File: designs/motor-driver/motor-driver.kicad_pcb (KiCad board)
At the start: 2 copper layers, 50 x 50 mm, 16 parts, among them IC1 ATMEGA168-P, P1 CONN_2, P2 ISP, P3 CONN_2, P4 CONN_2, P5 CONN_2, P6 CONN_2, U1 TB6552FNG, U2 TB6552FNG, X1 CRYSTAL_RESONATOR

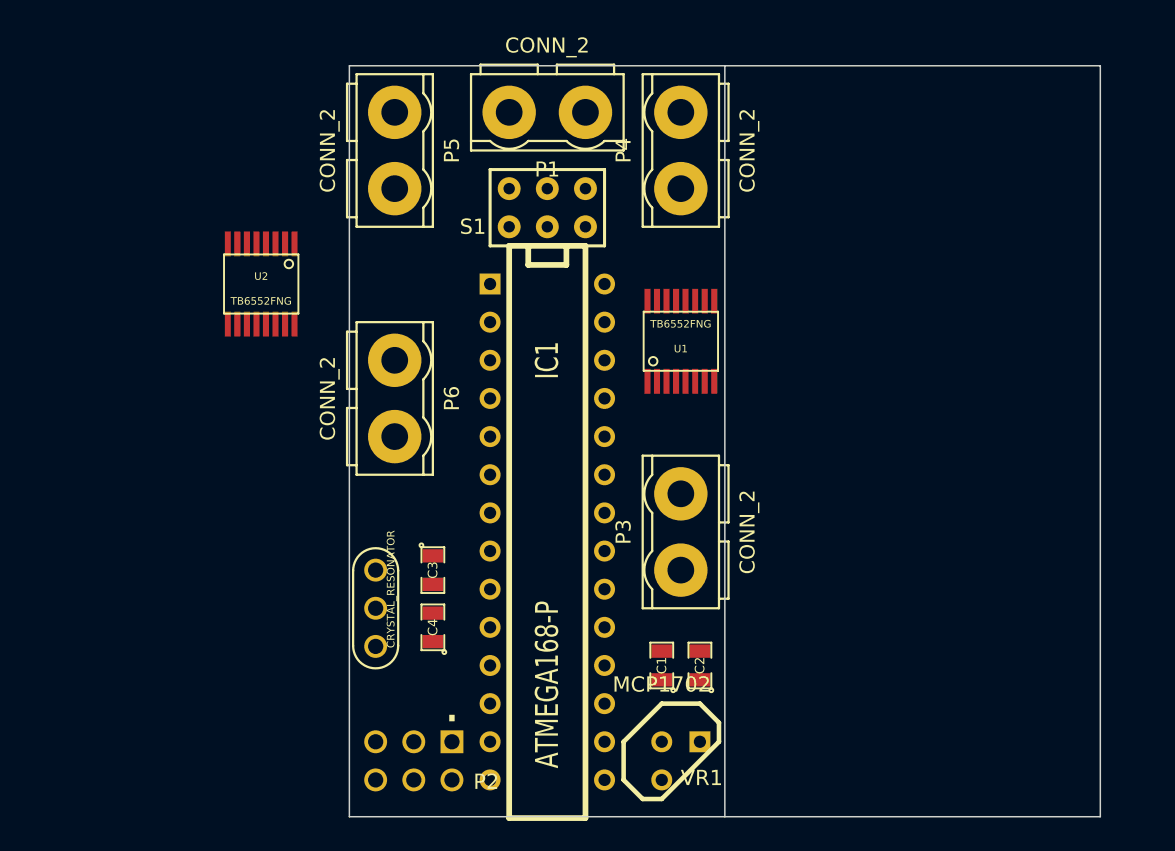
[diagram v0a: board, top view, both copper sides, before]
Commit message: Changed to L293D chip... a bit easier to work with, and has tons of support with AVR / Arduino code.
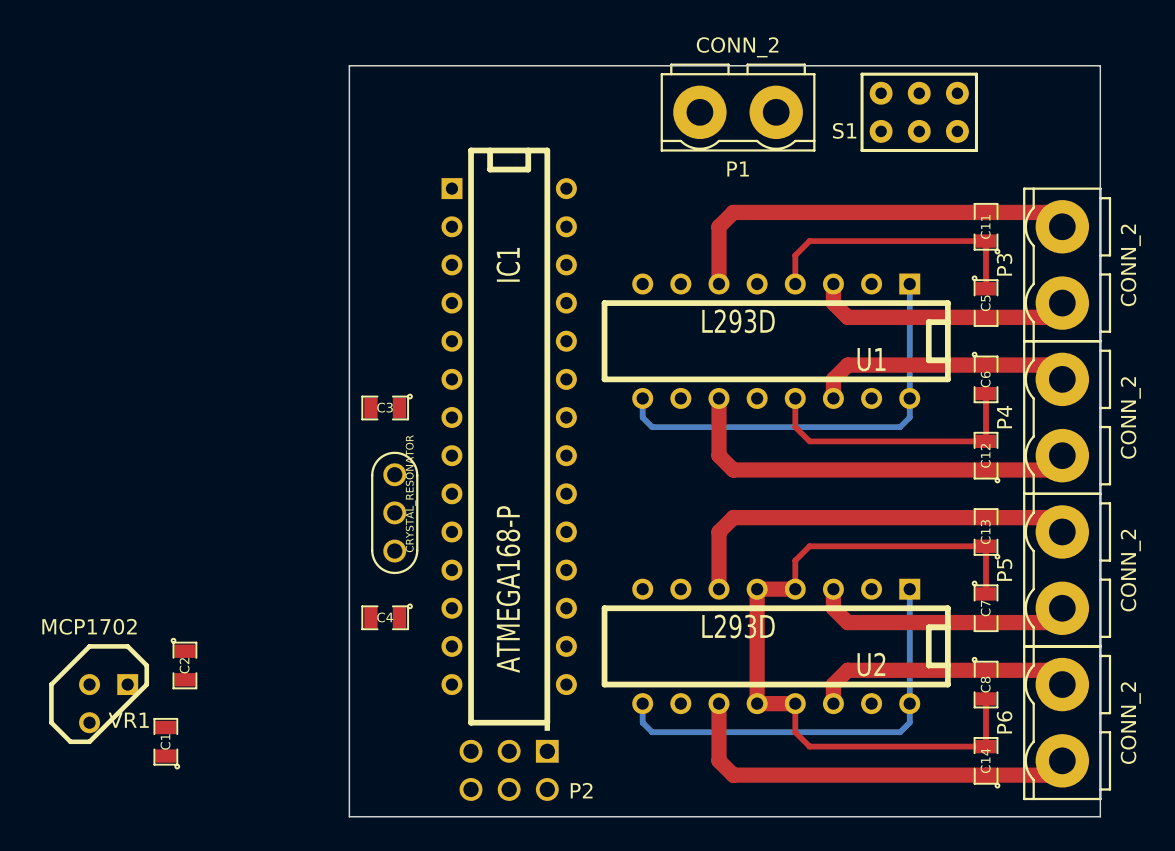
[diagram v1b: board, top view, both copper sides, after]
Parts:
- added C11: 0.1uF, SM0805, F.Cu at (72.4, 45.7)
- added C12: 0.1uF, SM0805, F.Cu at (72.4, 61.0)
- added C13: 0.1uF, SM0805, F.Cu at (72.4, 66.0)
- added C14: 0.1uF, SM0805, F.Cu at (72.4, 81.3)
- added C5: 0.1uF, SM0805, F.Cu at (72.4, 50.8)
- added C6: 0.1uF, SM0805, F.Cu at (72.4, 55.9)
- added C7: 0.1uF, SM0805, F.Cu at (72.4, 71.1)
- added C8: 0.1uF, SM0805, F.Cu at (72.4, 76.2)
- U1, U2: value TB6552FNG -> L293D; footprint ssop-16 -> DIP-16__300
- moved P5 52.5 mm to (77.5, 68.6), turned to 90 degrees
- moved P6 49.4 mm to (77.5, 78.7), turned to 90 degrees
- moved U2 41.9 mm to (58.4, 73.7)
- moved VR1 38.3 mm to (14.0, 77.5)
- moved C2 34.3 mm to (19.1, 74.9), turned to 270 degrees
- moved C1 33.4 mm to (17.8, 80.0)
- moved P3 31.0 mm to (77.5, 48.3)
- moved P4 31.0 mm to (77.5, 58.4)
- moved S1 25.6 mm to (67.9, 38.1)
- moved P1 12.7 mm to (55.9, 38.1)
- moved C3 11.3 mm to (32.4, 57.8), turned to 180 degrees
- moved IC1 6.84 mm to (40.6, 59.7)
- moved X1 6.48 mm to (33.0, 64.8)
- moved P2 6.38 mm to (40.6, 81.9)
- moved U1 6.35 mm to (58.4, 53.3), turned to 180 degrees
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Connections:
- net /AIN1 renamed /MOTOR1_1A
- net /BO1 renamed /MOTOR2_3Y
- net /DO1 renamed /MOTOR4_3Y
- net N-000004 renamed /VREG_IN
- C1 pad 1: +3.3V -> /VREG_OUT
- IC1 pad 11: /DIN1 -> (no net)
- IC1 pad 12: /DIN2 -> (no net)
- IC1 pad 13: /DPWM -> (no net)
- IC1 pad 15: /APWM -> /MOTOR2_4A
- IC1 pad 16: /AIN2 -> /MOTOR2_3A
- IC1 pad 23: /BIN1 -> /MOTOR1_2A
- IC1 pad 24: /BIN2 -> /MOTOR3_1A
- IC1 pad 25: /BPWM -> /MOTOR3_2A
- IC1 pad 26: (no net) -> /MOTOR4_3A
- IC1 pad 4: /CIN1 -> (no net)
- IC1 pad 5: /CIN2 -> /MOTOR4_4A
- IC1 pad 6: /CPWM -> (no net)
- P3 pad 1: /AO1 -> /MOTOR1_1Y
- P3 pad 2: /AO2 -> /MOTOR1_2Y
- P4 pad 2: /BO2 -> /MOTOR2_4Y
- P5 pad 1: /CO1 -> /MOTOR3_1Y
- P5 pad 2: /CO2 -> /MOTOR3_2Y
- P6 pad 2: /DO2 -> /MOTOR4_4Y
- S1 pad 6: +3.3V -> /VREG_OUT
- U1 pad 1: GND -> +5V
- U1 pad 10: /BO2 -> /MOTOR2_3A
- U1 pad 12: +3.3V -> GND
- U1 pad 13: /BPWM -> GND
- U1 pad 14: /BIN2 -> /MOTOR2_4Y
- U1 pad 15: /BIN1 -> /MOTOR2_4A
- U1 pad 16: +3.3V -> +5V
- U1 pad 3: /AIN2 -> /MOTOR1_1Y
- U1 pad 4: /APWM -> GND
- U1 pad 5: +3.3V -> GND
- U1 pad 6: +6V -> /MOTOR1_2Y
- U1 pad 7: /AO1 -> /MOTOR1_2A
- U1 pad 8: /AO2 -> +BATT
- U1 pad 9: AGND -> +5V
- U2 pad 1: GND -> +5V
- U2 pad 10: /DO2 -> /MOTOR4_3A
- U2 pad 12: +3.3V -> GND
- U2 pad 13: /DPWM -> GND
- U2 pad 14: /DIN2 -> /MOTOR4_4Y
- U2 pad 15: /DIN1 -> /MOTOR4_4A
- U2 pad 16: +3.3V -> +5V
- U2 pad 2: /CIN1 -> /MOTOR3_1A
- U2 pad 3: /CIN2 -> /MOTOR3_1Y
- U2 pad 4: /CPWM -> GND
- U2 pad 5: +3.3V -> GND
- U2 pad 6: +6V -> /MOTOR3_2Y
- U2 pad 7: /CO1 -> /MOTOR3_2A
- U2 pad 8: /CO2 -> +BATT
- U2 pad 9: AGND -> +5V
- VR1 pad 3: +3.3V -> /VREG_OUT
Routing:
- net GND: track 0.00 -> 85.4 mm
- net +5V: track 0.00 -> 56.9 mm
- net /MOTOR4_3Y: track 0.00 -> 27.5 mm
- net /MOTOR2_3Y: track 0.00 -> 27.5 mm
- net /MOTOR1_2Y: track 0.00 -> 27.5 mm
- net /MOTOR3_2Y: track 0.00 -> 27.5 mm
- net /MOTOR3_1Y: track 0.00 -> 17.3 mm
- net /MOTOR4_4Y: track 0.00 -> 17.3 mm
- net /MOTOR2_4Y: track 0.00 -> 17.3 mm
- net /MOTOR1_1Y: track 0.00 -> 17.3 mm
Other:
- outline, holes or cut-outs redrawn
- net class Default: clearance 0.254 -> 0.381; trace_width 0.254 -> 0.381
- rule trace_clearance: 0.254 -> 0.381
- rule trace_min: 0.254 -> 0.381

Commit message: annoying through hole, 5v components...
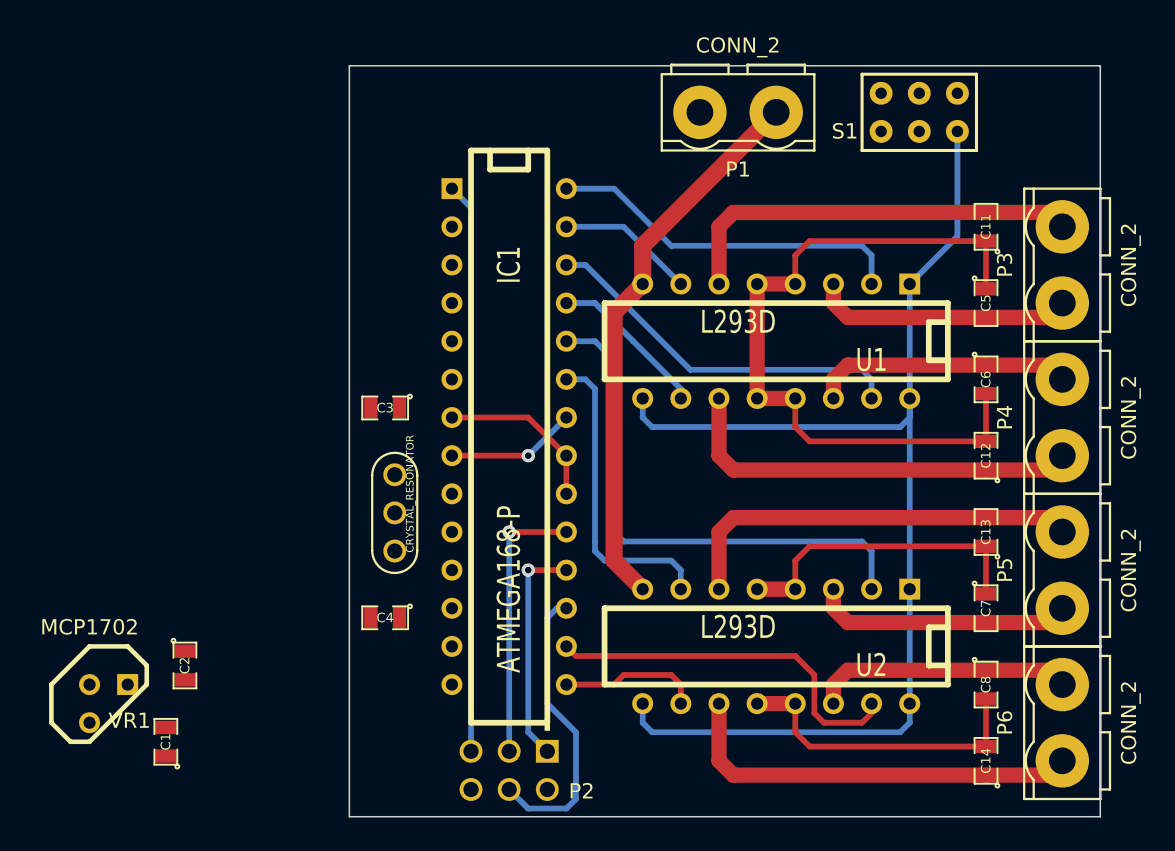
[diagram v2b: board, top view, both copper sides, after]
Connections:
- net N-0000032 renamed /PROG_VCC
- C1 pad 1: /VREG_OUT -> +5V
- IC1 pad 14: /MOTOR1_1A -> (no net)
- IC1 pad 15: /MOTOR2_4A -> /MOTOR4_3A
- IC1 pad 16: /MOTOR2_3A -> /MOTOR4_4A
- IC1 pad 23: /MOTOR1_2A -> /MOTOR3_2A
- IC1 pad 25: /MOTOR3_2A -> /MOTOR2_3A
- IC1 pad 26: /MOTOR4_3A -> /MOTOR2_4A
- IC1 pad 27: (no net) -> /MOTOR1_2A
- IC1 pad 28: (no net) -> /MOTOR1_1A
- IC1 pad 5: /MOTOR4_4A -> (no net)
- S1 pad 6: /VREG_OUT -> +5V
- VR1 pad 3: /VREG_OUT -> +5V
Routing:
- net /RESET: track 0.00 -> 38.0 mm
- net +BATT: track 0.00 -> 37.0 mm
- net /MOTOR3_1A: track 0.00 -> 35.3 mm
- net /MOTOR4_4A: track 0.00 -> 24.8 mm
- net /MOTOR2_4A: track 0.00 -> 24.7 mm
- net +5V: track 56.9 -> 81.1 mm
- net /MOTOR1_1A: track 0.00 -> 24.1 mm
- net /MOTOR3_2A: track 0.00 -> 20.5 mm
- net /MOSI: track 0.00 -> 19.6 mm
- net /SCK: track 0.00 -> 18.4 mm, vias 0 -> 1
- net /MISO: track 0.00 -> 15.1 mm, vias 0 -> 1
- net GND: track 85.4 -> 99.2 mm, vias 0 -> 1
- net VCC: track 0.00 -> 11.2 mm
- net /MOTOR2_3A: track 0.00 -> 10.6 mm
- net /MOTOR4_3A: track 0.00 -> 9.42 mm
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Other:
- net class Default: clearance 0.381 -> 0.254
- rule trace_clearance: 0.381 -> 0.254

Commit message: WIP motor driver... adding XBee, optional 5v regulator, etc
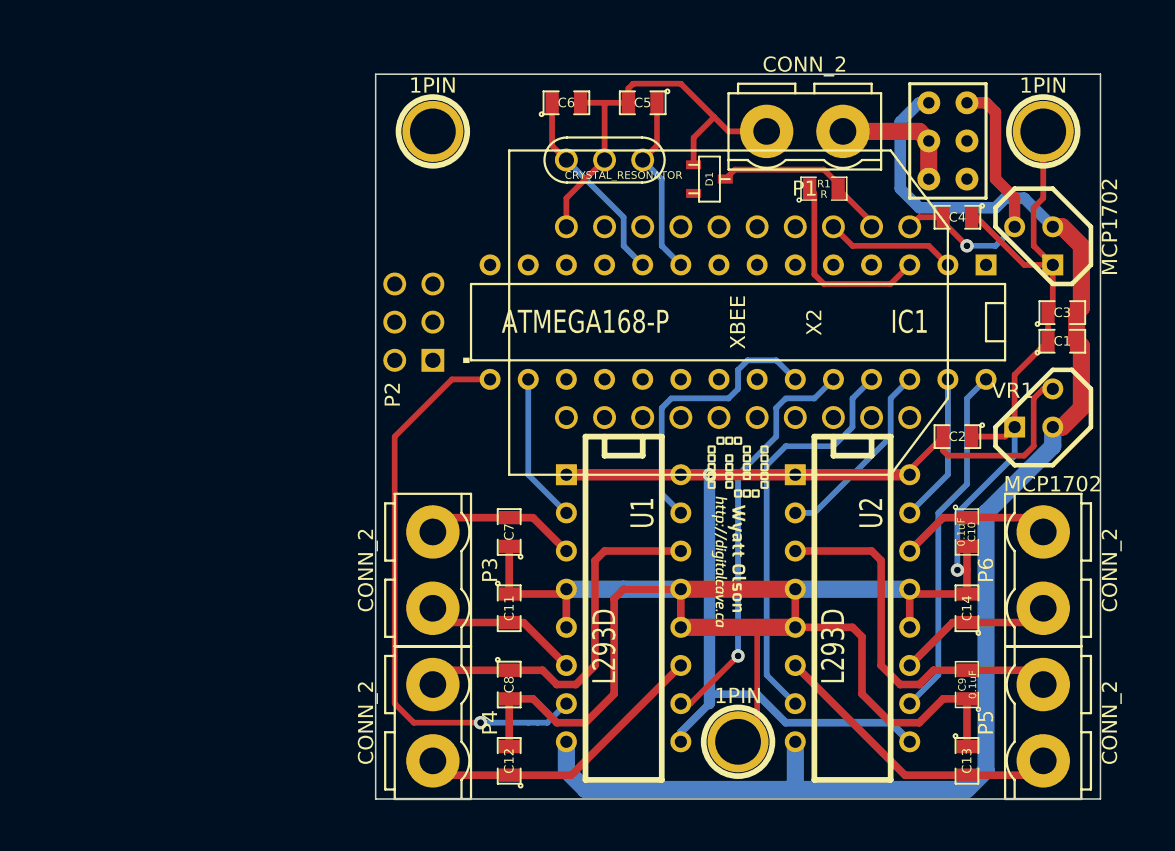
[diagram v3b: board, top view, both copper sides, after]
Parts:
- added 1PIN: P***, 1pin, F.Cu at (55.9, 80.0)
- added 1PIN: P***, 1pin, F.Cu at (35.6, 39.4)
- added 1PIN: P***, 1pin, F.Cu at (76.2, 39.4)
- added C10: 0.1uF, SM0805, F.Cu at (71.1, 66.0)
- added C9: 0.1uF, SM0805, F.Cu at (71.1, 76.2)
- added D1: ZENER, sot23, F.Cu at (54.0, 42.5)
- added R1: R, SM0805, F.Cu at (61.6, 43.2)
- added VAL: DIGITALCAVE_LOGO_WIDE_SMALL, DIGITALCAVE_LOGO_WIDE_SMALL, F.Cu at (55.9, 66.0)
- added VR2: MCP1702, TO92, F.Cu at (75.6, 47.0)
- added X2: XBEE, XBEE_SPARKFUN_BREAKOUT, F.Cu at (55.9, 52.1)
- C1, C2, C3, C4: value C -> 1uF
- C5, C6: value 0.1uF -> 20pF
- moved C1 65.4 mm to (77.5, 53.3), turned to 0 degrees
- moved VR1 64.7 mm to (75.6, 57.8), turned to 180 degrees
- moved C2 53.6 mm to (70.5, 59.7), turned to 180 degrees
- moved P3 46.6 mm to (35.6, 68.6), turned to 270 degrees
- moved P4 46.6 mm to (35.6, 78.7), turned to 270 degrees
- moved C4 46.5 mm to (70.5, 45.1)
- moved C3 45.5 mm to (77.5, 51.4), turned to 0 degrees
- moved C11 40.7 mm to (40.6, 71.1), turned to 270 degrees
- moved C12 37.7 mm to (40.6, 81.3)
- moved C6 33.5 mm to (44.5, 37.5), turned to 0 degrees
- moved C7 32.2 mm to (40.6, 66.0), turned to 90 degrees
- moved C8 31.8 mm to (40.6, 76.2)
- moved P2 30.5 mm to (34.3, 52.1), turned to 90 degrees
- moved X1 27.3 mm to (47.0, 41.3), turned to 180 degrees
- moved C5 26.5 mm to (49.5, 37.5), turned to 180 degrees
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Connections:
- net /PROG_VCC renamed N-0000011
- net VCC renamed N-0000047
- C1 pad 1: +5V -> GND
- C1 pad 2: GND -> +BATT
- C2 pad 1: /VREG_IN -> GND
- C2 pad 2: GND -> +5V
- C3 pad 1: /XTAL1 -> GND
- C3 pad 2: GND -> +BATT
- C4 pad 1: /XTAL2 -> GND
- C4 pad 2: GND -> +3.3V
- C5 pad 1: GND -> /XTAL1
- C5 pad 2: /MOTOR1_1Y -> GND
- C6 pad 1: /MOTOR2_4Y -> /XTAL2
- C7 pad 2: /MOTOR3_1Y -> /MOTOR1_1Y
- C8 pad 1: /MOTOR4_4Y -> /MOTOR2_4Y
- IC1 pad 15: /MOTOR4_3A -> /MOTOR1_2A
- IC1 pad 16: /MOTOR4_4A -> /MOTOR1_1A
- IC1 pad 2: (no net) -> N-0000037
- IC1 pad 23: /MOTOR3_2A -> /MOTOR2_4A
- IC1 pad 24: /MOTOR3_1A -> /MOTOR2_3A
- IC1 pad 25: /MOTOR2_3A -> /MOTOR3_2A
- IC1 pad 26: /MOTOR2_4A -> /MOTOR3_1A
- IC1 pad 27: /MOTOR1_2A -> /MOTOR4_4A
- IC1 pad 28: /MOTOR1_1A -> /MOTOR4_3A
- IC1 pad 3: (no net) -> N-0000019
- P1 pad 1: +BATT -> N-0000039
- P4 pad 1: /MOTOR2_3Y -> /MOTOR2_4Y
- P4 pad 2: /MOTOR2_4Y -> /MOTOR2_3Y
- P5 pad 1: /MOTOR3_1Y -> /MOTOR3_2Y
- P5 pad 2: /MOTOR3_2Y -> /MOTOR3_1Y
- S1 pad 1: /VREG_IN -> N-0000039
- S1 pad 2: +BATT -> N-0000039
- S1 pad 3: (no net) -> +BATT
- S1 pad 6: +5V -> +3.3V
- VR1 pad 2: /VREG_IN -> +BATT
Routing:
- net GND: track 99.2 -> 176.7 mm
- net +BATT: track 37.0 -> 93.3 mm
- net /RESET: track 38.0 -> 0.00 mm
- net /MOTOR1_2A: track 9.20 -> 38.2 mm, vias 0 -> 1
- net /MOTOR3_1A: track 35.3 -> 12.8 mm
- net /MOSI: track 19.6 -> 0.00 mm
- net +3.3V: track 0.00 -> 19.1 mm, vias 0 -> 1
- net /SCK: track 18.4 -> 0.00 mm, vias 1 -> 0
- net /MOTOR4_3Y: track 27.5 -> 10.5 mm
- net /MOTOR1_2Y: track 27.5 -> 10.5 mm
- net /MOTOR2_3A: track 10.6 -> 27.3 mm, vias 0 -> 1
- net /MISO: track 15.1 -> 0.00 mm, vias 1 -> 0
- net /MOTOR4_4A: track 24.8 -> 9.94 mm
- net /MOTOR4_3A: track 9.42 -> 23.7 mm
- net /MOTOR1_1A: track 24.1 -> 9.94 mm
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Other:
- board size 50 x 50 mm -> 48.3 x 48.3 mm

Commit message: More updates to motor circuit.  Finished adding XBee, added LED, cleaned up text, etc.
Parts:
- removed the 1PIN at (35.6, 39.4)
- added D2: LED, LED-5MM, F.Cu at (36.2, 59.7)
- added P7: CONN_7, PIN_ARRAY_7x1, F.Cu at (54.6, 37.5)
- added R2: 1k, SM0805, F.Cu at (40.6, 59.1)
- D1: value ZENER -> ZD 3v3
- P1: value CONN_2 -> BATT
- P3: value CONN_2 -> MOTOR_1
- P4: value CONN_2 -> MOTOR_2
- P5: value CONN_2 -> MOTOR_3
- P6: value CONN_2 -> MOTOR_4
- R1: value R -> 1k
- VR1, VR2: footprint TO92 -> TO92_SMALL
- moved 1PIN 21.7 mm to (54.6, 41.3)
- moved P1 16.6 mm to (76.8, 41.3), turned to 90 degrees
- moved C5 11.0 mm to (38.7, 39.4)
- moved C3 10.8 mm to (78.1, 62.2)
- moved X1 10.3 mm to (36.8, 43.2)
- moved C4 10.0 mm to (76.2, 53.3), turned to 0 degrees
- moved C6 9.71 mm to (34.9, 39.4)
- moved C1 9.53 mm to (71.8, 45.7), turned to 180 degrees
- moved D1 8.25 mm to (62.2, 42.5)
- moved C2 4.58 mm to (74.3, 62.2)
- moved R1 4.49 mm to (66.0, 42.5), turned to 180 degrees
- moved VAL 3.81 mm to (55.9, 69.8), turned to 90 degrees
- moved VR2 2.62 mm to (76.2, 49.5)
- moved S1 1.27 mm to (71.1, 40.0), turned to 270 degrees
- moved VR1 0.64 mm to (76.2, 57.8), turned to 270 degrees
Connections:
- net N-0000011 renamed /PROG_VCC
- net N-0000019 renamed /TX
- net N-0000047 renamed /AVR_VCC
- D1 pad 2: N-0000018 -> N-0000034
- IC1 pad 11: (no net) -> /MOTOR2_4A
- IC1 pad 2: N-0000037 -> /RX
- IC1 pad 23: /MOTOR2_4A -> /ADC0
- IC1 pad 24: /MOTOR2_3A -> /ADC1
- IC1 pad 25: /MOTOR3_2A -> /MOTOR4_3A
- IC1 pad 26: /MOTOR3_1A -> /MOTOR4_4A
- IC1 pad 27: /MOTOR4_4A -> /SDA
- IC1 pad 28: /MOTOR4_3A -> /SCL
- IC1 pad 4: (no net) -> /MOTOR3_1A
- IC1 pad 5: (no net) -> /MOTOR3_2A
- IC1 pad 6: (no net) -> /MOTOR2_3A
- P1 pad 1: N-0000039 -> GND
- P1 pad 2: GND -> /BATTERY
- R1 pad 2: N-0000018 -> N-0000034
- S1 pad 1: N-0000039 -> /BATTERY
- S1 pad 2: N-0000039 -> /BATTERY
- X2 pad 2: N-0000018 -> /RX
- X2 pad 3: N-0000037 -> N-0000034
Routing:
- net +BATT: track 93.3 -> 169.9 mm
- net GND: track 176.7 -> 243.2 mm, vias 1 -> 2
- net /PROG_VCC: track 0.00 -> 60.4 mm, vias 0 -> 2
- net /RESET: track 0.00 -> 39.9 mm, vias 0 -> 1
- net /AVR_VCC: track 0.00 -> 35.0 mm, vias 0 -> 1
- net /SCL: track 0.00 -> 30.0 mm, vias 0 -> 2
- net /SDA: track 0.00 -> 29.6 mm, vias 0 -> 2
- net /ADC1: track 0.00 -> 27.1 mm, vias 0 -> 2
- net /ADC0: track 0.00 -> 26.3 mm, vias 0 -> 2
- net +3.3V: track 19.1 -> 44.3 mm, vias 1 -> 0
- net /SCK: track 0.00 -> 17.8 mm, vias 0 -> 1
- net /MOSI: track 0.00 -> 14.1 mm, vias 0 -> 1
- net /MISO: track 0.00 -> 12.3 mm
- net N-0000018: track 12.0 -> 0.00 mm
- net /XTAL2: track 13.3 -> 24.9 mm
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- added copper zone on B.Cu, net GND
- added copper zone on F.Cu, net GND
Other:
- board text added: "+"
- board text added: "-"
- board text added: "3v3"
- board text added: "ADC0"
- board text added: "ADC1"
- board text added: "BATT"
- board text added: "GND"
- board text added: "OFF"
- board text added: "ON"
- board text added: "SCL"
- board text added: "SDA"
